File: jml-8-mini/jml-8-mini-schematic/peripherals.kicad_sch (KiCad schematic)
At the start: 8 parts, among them J2 SIO CHB, J3 UART, J4 CTC EXTRA LINES, U4 Z80 CTC, U5 Z80 SIO

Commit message: update info section of schematic
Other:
- company: https://github.com/jac-oblong/jml -> https://github.com/jac-oblong/JML
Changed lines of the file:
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@@
     (date "2023-10-02")
     (rev "A")
-    (company "https://github.com/jac-oblong/jml")
+    (company "https://github.com/jac-oblong/JML")
     (comment 1 "Design of Z80 based microcomputer")
     (comment 3 "Released under MIT License")

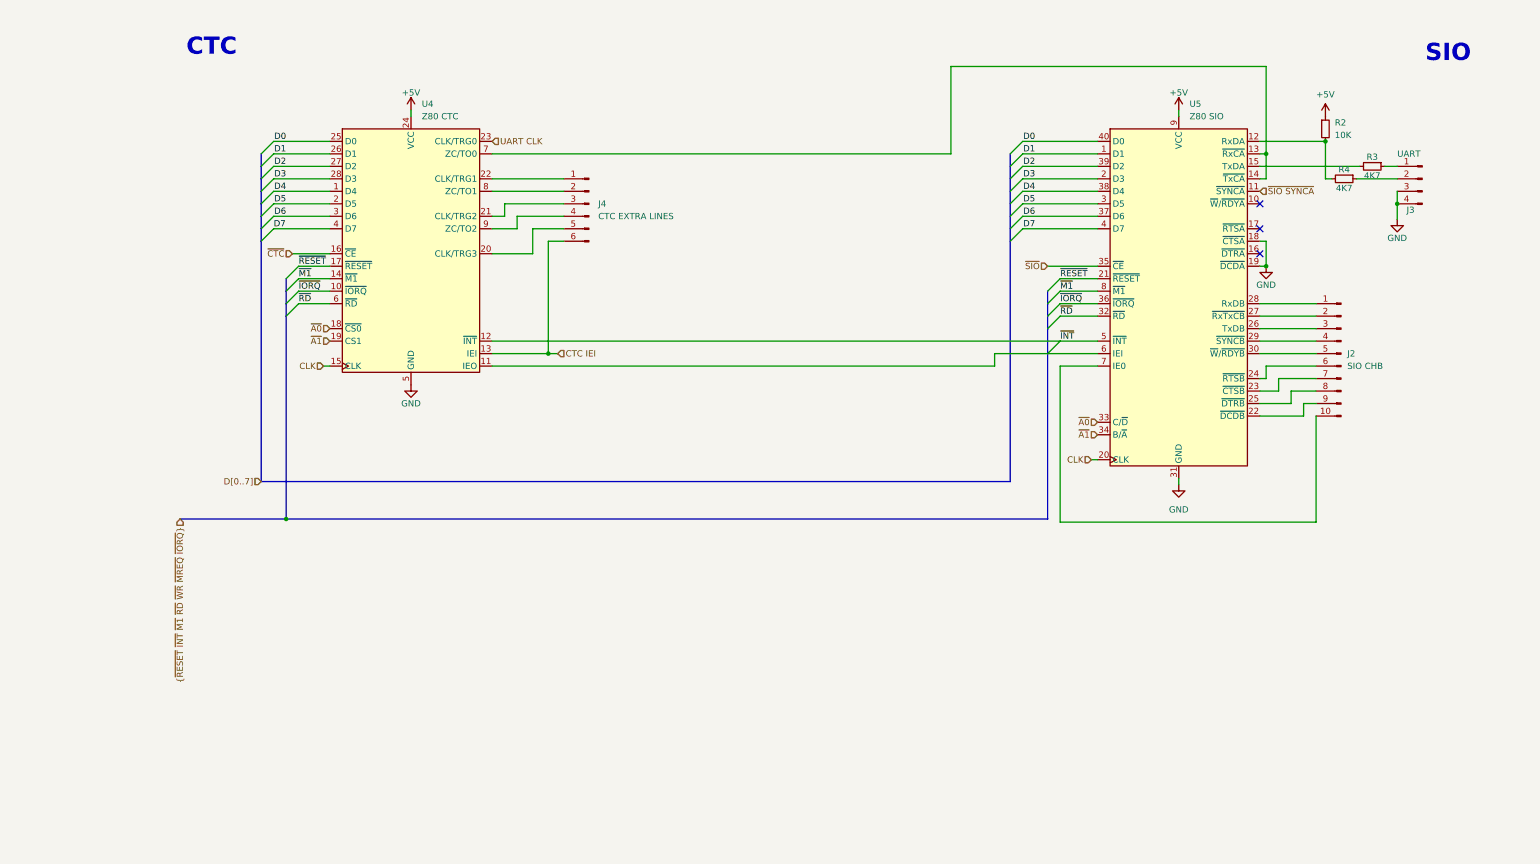
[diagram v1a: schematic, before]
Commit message: general "neatening" of schematics
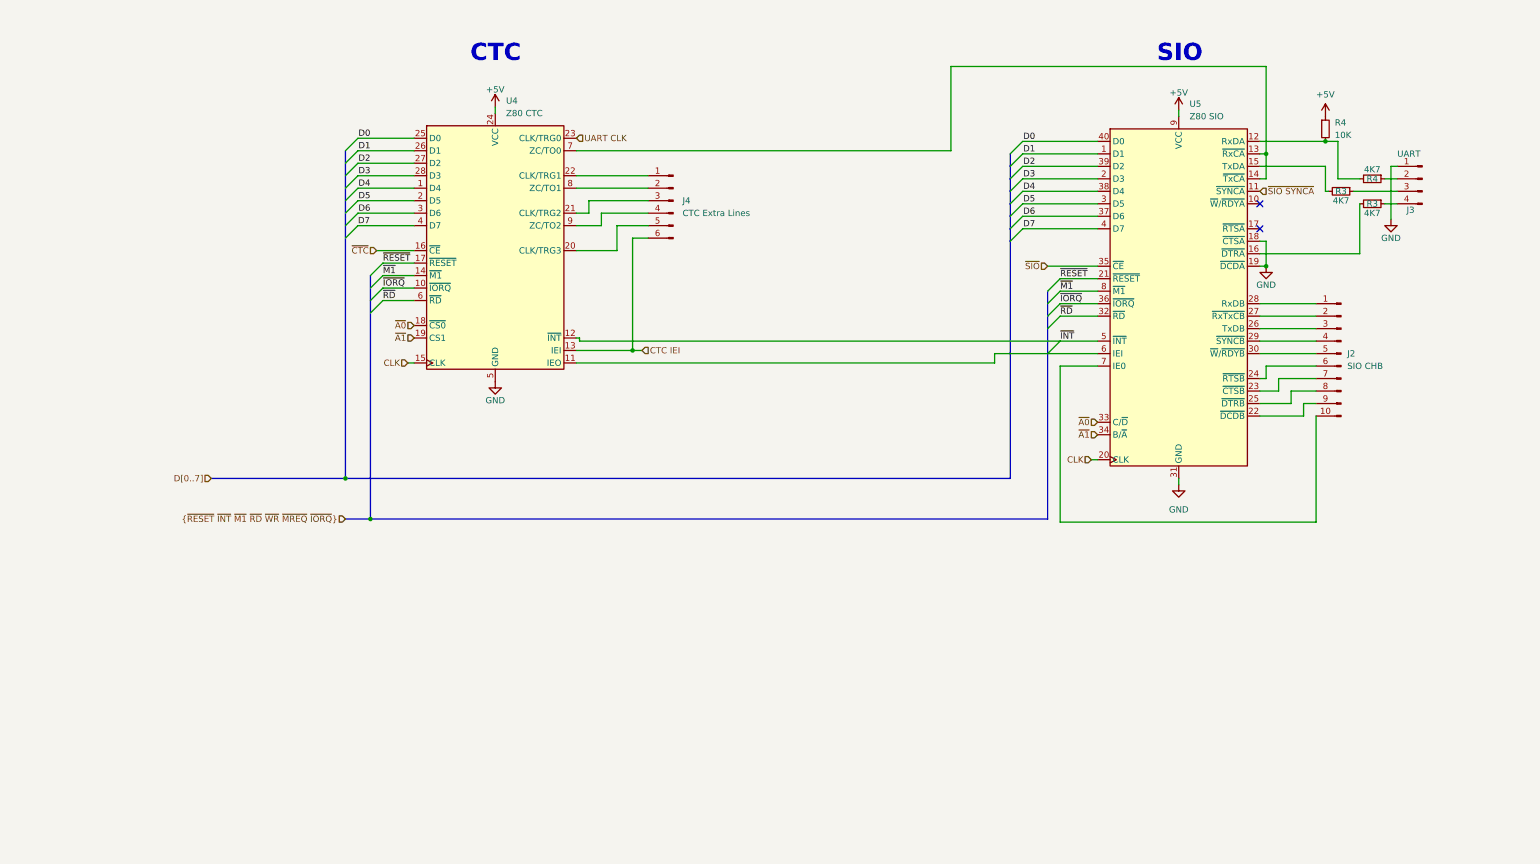
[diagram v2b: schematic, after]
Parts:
- added R3: 4K7, Resistor_THT:R_Axial_DIN0207_L6.3mm_D2.5mm_P10.16mm_Horizontal, symbol Device:R_Small
- J4: value CTC EXTRA LINES -> CTC Extra Lines
- renumbered R2 to R4
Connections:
- net GND: now also J3.1 (Pin_1); no longer J3.3 (Pin_3), J3.4 (Pin_4)
- net at R3.1: now also J3.3 (Pin_3); no longer J3.1 (Pin_1)
- net at U5.16 (~{DTRA}): now also R3.2
- new net: J3.4 (Pin_4), R3.1
- no-connect marks 3 -> 2
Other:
- moved on the sheet: J4, R3, R4, U4

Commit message: change some footprints
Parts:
- R3, R4: footprint Resistor_THT:R_Axial_DIN0207_L6.3mm_D2.5mm_P10.16mm_Horizontal -> Resistor_THT:R_Axial_DIN0207_L6.3mm_D2.5mm_P7.62mm_Horizontal
- U4: footprint Package_DIP:DIP-28_W15.24mm_LongPads -> Package_DIP:DIP-28_W15.24mm_Socket_LongPads
- U5: footprint Package_DIP:DIP-40_W15.24mm_LongPads -> Package_DIP:DIP-40_W15.24mm_Socket_LongPads
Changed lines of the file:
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@@
       (effects (font (size 1.27 1.27)))
     )
-    (property "Footprint" "Resistor_THT:R_Axial_DIN0207_L6.3mm_D2.5mm_P10.16mm_Horizontal" (at 257.81 51.435 0)
+    (property "Footprint" "Resistor_THT:R_Axial_DIN0207_L6.3mm_D2.5mm_P7.62mm_Horizontal" (at 257.81 51.435 0)
       (effects (font (size 1.27 1.27)) hide)
     )
@@
       (effects (font (size 1.27 1.27)))
     )
-    (property "Footprint" "Resistor_THT:R_Axial_DIN0207_L6.3mm_D2.5mm_P10.16mm_Horizontal" (at 257.81 46.355 0)
+    (property "Footprint" "Resistor_THT:R_Axial_DIN0207_L6.3mm_D2.5mm_P7.62mm_Horizontal" (at 257.81 46.355 0)
       (effects (font (size 1.27 1.27)) hide)
     )
@@
       (effects (font (size 1.27 1.27)) (justify left))
     )
-    (property "Footprint" "Resistor_THT:R_Axial_DIN0207_L6.3mm_D2.5mm_P10.16mm_Horizontal" (at 248.285 36.195 0)
+    (property "Footprint" "Resistor_THT:R_Axial_DIN0207_L6.3mm_D2.5mm_P7.62mm_Horizontal" (at 248.285 36.195 0)
       (effects (font (size 1.27 1.27)) hide)
     )
@@
       (effects (font (size 1.27 1.27)))
     )
-    (property "Footprint" "Resistor_THT:R_Axial_DIN0207_L6.3mm_D2.5mm_P10.16mm_Horizontal" (at 251.46 48.895 0)
+    (property "Footprint" "Resistor_THT:R_Axial_DIN0207_L6.3mm_D2.5mm_P7.62mm_Horizontal" (at 251.46 48.895 0)
       (effects (font (size 1.27 1.27)) hide)
     )
@@
       (effects (font (size 1.27 1.27)) (justify left))
     )
-    (property "Footprint" "Package_DIP:DIP-40_W15.24mm_LongPads" (at 224.79 81.915 0)
+    (property "Footprint" "Package_DIP:DIP-40_W15.24mm_Socket_LongPads" (at 224.79 81.915 0)
       (effects (font (size 1.27 1.27)) hide)
     )
@@
       (effects (font (size 1.27 1.27)) (justify left))
     )
-    (property "Footprint" "Package_DIP:DIP-28_W15.24mm_LongPads" (at 79.375 58.42 0)
-      (effects (font (size 1.27 1.27)) hide)
-    )
+    (property "Footprint" "Package_DIP:DIP-28_W15.24mm_Socket_LongPads" (at 79.375 58.42 0)
+      (effects (font (size 1.27 1.27)) hide)
+    )

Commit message: lots of updates to schematic to make pcb routing easier, start on pcb design
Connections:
- net UART_CTS: now reaches J3.4 (Pin_4), R3.1
- net ~{DTRA}: now reaches R3.2, U5.16 (~{DTRA})
- net UART_Tx: now reaches J3.2 (Pin_2), R4.1
- net RxDA: now reaches R4.2, R4.2, U5.12 (RxDA)
- net CLK/TRG1: now reaches J4.1 (Pin_1), U4.22 (CLK/TRG1)
- net ZC/TO1: now reaches J4.2 (Pin_2), U4.8 (ZC/TO1)
- net CLK/TRG2: now reaches J4.3 (Pin_3), U4.21 (CLK/TRG2)
- net CLK/TRG3: now reaches J4.4 (Pin_4)
- net CLK/TRG3: now also U4.20 (CLK/TRG3); no longer U4.9 (ZC/TO2)
- net ZC/TO2: now reaches J4.5 (Pin_5)
- net ZC/TO2: now also U4.9 (ZC/TO2); no longer U4.20 (CLK/TRG3)
- net UART_Rx: now reaches J3.3 (Pin_3), R3.1
- net TxDA: now reaches R3.2, U5.15 (TxDA)
- net CTC_IEO: now reaches J2.1 (Pin_1)
- net CTC_IEO: now also U5.7 (IE0); no longer U5.28 (RxDB)
- net ~{DCDB}: now reaches J2.10 (Pin_10)
- net ~{DCDB}: now also U5.22 (~{DCDB}); no longer U5.7 (IE0)
- net ~{RxTxCB}: now reaches U5.27 (~{RxTxCB})
- net ~{RxTxCB}: now also J2.5 (Pin_5); no longer J2.2 (Pin_2)
- net TxDB: now reaches U5.26 (TxDB)
- net TxDB: now also J2.6 (Pin_6); no longer J2.3 (Pin_3)
- net RxDB: now reaches J2.4 (Pin_4)
- net RxDB: now also U5.28 (RxDB); no longer U5.29 (~{SYNCB})
- net ~{W}/~{RDYB}: now reaches U5.30 (~{W}/~{RDYB})
- net ~{W}/~{RDYB}: now also J2.2 (Pin_2); no longer J2.5 (Pin_5)
- net ~{RTSB}: now reaches U5.24 (~{RTSB})
- net ~{RTSB}: now also J2.8 (Pin_8); no longer J2.6 (Pin_6)
- net ~{CTSB}: now reaches U5.23 (~{CTSB})
- net ~{CTSB}: now also J2.9 (Pin_9); no longer J2.7 (Pin_7)
- net ~{DTRB}: now reaches U5.25 (~{DTRB})
- net ~{DTRB}: now also J2.7 (Pin_7); no longer J2.8 (Pin_8)
- net SIO_UART_CLK: now reaches U4.7 (ZC/TO0), U5.13 (~{RxCA}), U5.14 (~{TxCA})
- net SIO_IEI: now reaches U4.11 (IEO), U5.6 (IEI)
- new net ~{SYNCB}: J2.3 (Pin_3), U5.29 (~{SYNCB})
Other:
- note added: "PERIPHERALS"
- note added: "Resistors limit current, and prevent one device from powering the other"
- moved on the sheet: J2, J3, J4, U4

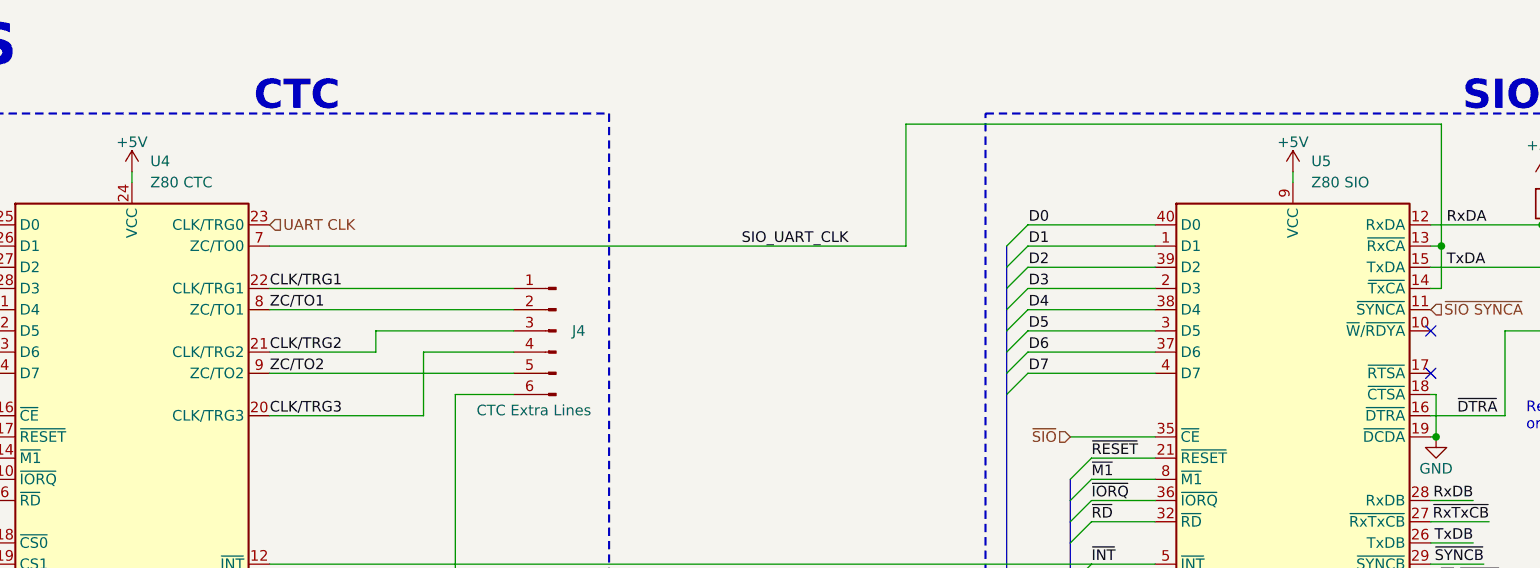
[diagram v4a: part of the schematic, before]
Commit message: complete PCB routing
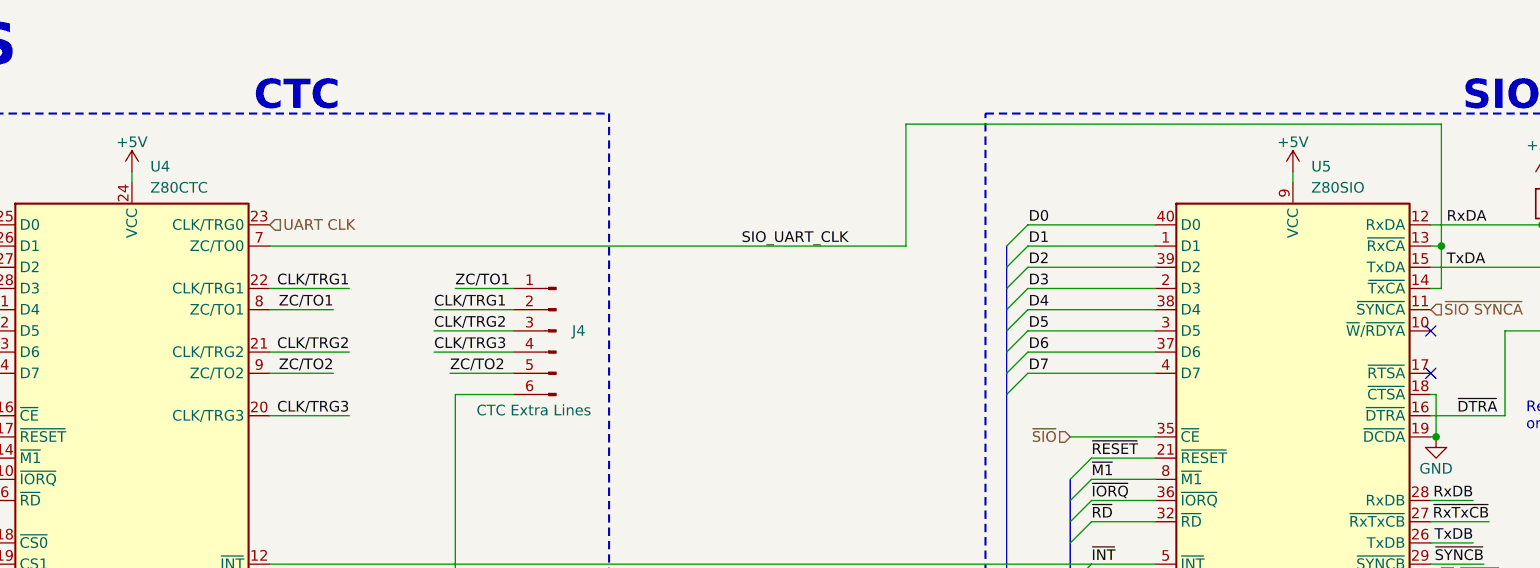
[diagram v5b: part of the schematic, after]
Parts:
- U4: value Z80 CTC -> Z80CTC
- U5: value Z80 SIO -> Z80SIO
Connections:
- net CLK/TRG1: now also J4.2 (Pin_2); no longer J4.1 (Pin_1)
- net ZC/TO1: now also J4.1 (Pin_1); no longer J4.2 (Pin_2)
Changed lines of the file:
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@@
-    (stroke (width 0) (type default))
-  )
-  (wire (pts (xy 114.3 61.595) (xy 95.885 61.595))
     (stroke (width 0) (type default))
   )
@@
     (stroke (width 0) (type default))
   )
-  (wire (pts (xy 95.885 46.355) (xy 125.095 46.355))
-    (stroke (width 0) (type default))
-  )
   (bus (pts (xy 48.895 107.315) (xy 48.895 59.055))
     (stroke (width 0) (type default))
@@
     (stroke (width 0) (type default))
   )
-  (wire (pts (xy 95.885 53.975) (xy 108.585 53.975))
-    (stroke (width 0) (type default))
-  )
   (bus (pts (xy 48.895 107.315) (xy 184.15 107.315))
     (stroke (width 0) (type default))
@@
     (stroke (width 0) (type default))
   )
-  (wire (pts (xy 95.885 48.895) (xy 125.095 48.895))
+  (wire (pts (xy 115.57 51.435) (xy 125.095 51.435))
     (stroke (width 0) (type default))
   )
@@
     (stroke (width 0) (type default))
   )
-  (wire (pts (xy 108.585 51.435) (xy 125.095 51.435))
-    (stroke (width 0) (type default))
-  )
   (wire (pts (xy 62.865 51.435) (xy 51.435 51.435))
     (stroke (width 0) (type default))
@@
     (stroke (width 0) (type default))
   )
+  (wire (pts (xy 115.57 48.895) (xy 125.095 48.895))
+    (stroke (width 0) (type default))
+  )
   (wire (pts (xy 56.515 64.135) (xy 62.865 64.135))
     (stroke (width 0) (type default))
@@
     (stroke (width 0) (type default))
   )
+  (wire (pts (xy 95.885 48.895) (xy 103.505 48.895))
+    (stroke (width 0) (type default))
+  )
   (wire (pts (xy 234.95 92.075) (xy 240.03 92.075))
     (stroke (width 0) (type default))
@@
     (stroke (width 0) (type default))
   )
+  (wire (pts (xy 117.475 56.515) (xy 125.095 56.515))
+    (stroke (width 0) (type default))
+  )
   (bus (pts (xy 48.895 46.355) (xy 48.895 48.895))
     (stroke (width 0) (type default))
@@
     (stroke (width 0) (type default))
   )
-  (wire (pts (xy 95.885 56.515) (xy 125.095 56.515))
+  (wire (pts (xy 95.885 53.975) (xy 105.41 53.975))
     (stroke (width 0) (type default))
   )
@@
     (stroke (width 0) (type default))
   )
+  (wire (pts (xy 115.57 53.975) (xy 125.095 53.975))
+    (stroke (width 0) (type default))
+  )
   (wire (pts (xy 248.285 43.815) (xy 234.95 43.815))
     (stroke (width 0) (type default))
@@
     (stroke (width 0) (type default))
   )
+  (wire (pts (xy 95.885 46.355) (xy 105.41 46.355))
+    (stroke (width 0) (type default))
+  )
   (wire (pts (xy 194.31 69.215) (xy 201.93 69.215))
     (stroke (width 0) (type default))
@@
     (stroke (width 0) (type default))
   )
-  (wire (pts (xy 108.585 53.975) (xy 108.585 51.435))
-    (stroke (width 0) (type default))
-  )
   (wire (pts (xy 260.985 92.075) (xy 255.27 92.075))
     (stroke (width 0) (type default))
   )
+  (wire (pts (xy 95.885 61.595) (xy 105.41 61.595))
+    (stroke (width 0) (type default))
+  )
   (wire (pts (xy 201.93 46.355) (xy 186.69 46.355))
     (stroke (width 0) (type default))
@@
     (stroke (width 0) (type default))
   )
+  (wire (pts (xy 118.11 46.355) (xy 125.095 46.355))
+    (stroke (width 0) (type default))
+  )
   (wire (pts (xy 254.635 76.835) (xy 260.985 76.835))
     (stroke (width 0) (type default))
   )
-  (wire (pts (xy 114.3 53.975) (xy 125.095 53.975))
-    (stroke (width 0) (type default))
-  )
-  (wire (pts (xy 114.3 53.975) (xy 114.3 61.595))
+  (wire (pts (xy 95.885 56.515) (xy 103.505 56.515))
     (stroke (width 0) (type default))
   )
@@
     (effects (font (size 1.27 1.27)) (justify left bottom))
   )
-  (label "CLK{slash}TRG3" (at 95.885 61.595 0) (fields_autoplaced)
-    (effects (font (size 1.27 1.27)) (justify left bottom))
+  (label "CLK{slash}TRG3" (at 105.41 61.595 180) (fields_autoplaced)
+    (effects (font (size 1.27 1.27)) (justify right bottom))
   )
   (label "D6" (at 189.23 53.975 180) (fields_autoplaced)
     (effects (font (size 1.27 1.27)) (justify right bottom))
   )
-  (label "CLK{slash}TRG2" (at 95.885 53.975 0) (fields_autoplaced)
-    (effects (font (size 1.27 1.27)) (justify left bottom))
+  (label "CLK{slash}TRG2" (at 105.41 53.975 180) (fields_autoplaced)
+    (effects (font (size 1.27 1.27)) (justify right bottom))
   )
   (label "TxDA" (at 236.855 43.815 0) (fields_autoplaced)
@@
     (effects (font (size 1.27 1.27)) (justify left bottom))
   )
+  (label "ZC{slash}TO1" (at 118.11 46.355 0) (fields_autoplaced)
+    (effects (font (size 1.27 1.27)) (justify left bottom))
+  )
   (label "D3" (at 189.23 46.355 180) (fields_autoplaced)
     (effects (font (size 1.27 1.27)) (justify right bottom))
@@
     (effects (font (size 1.27 1.27)) (justify right bottom))
   )
-  (label "ZC{slash}TO2" (at 95.885 56.515 0) (fields_autoplaced)
-    (effects (font (size 1.27 1.27)) (justify left bottom))
-  )
-  (label "CLK{slash}TRG1" (at 95.885 46.355 0) (fields_autoplaced)
-    (effects (font (size 1.27 1.27)) (justify left bottom))
+  (label "ZC{slash}TO2" (at 103.505 56.515 180) (fields_autoplaced)
+    (effects (font (size 1.27 1.27)) (justify right bottom))
+  )
+  (label "CLK{slash}TRG1" (at 105.41 46.355 180) (fields_autoplaced)
+    (effects (font (size 1.27 1.27)) (justify right bottom))
   )
   (label "~{IORQ}" (at 56.515 69.215 0) (fields_autoplaced)
@@
     (effects (font (size 1.27 1.27)) (justify left bottom))
   )
+  (label "CLK{slash}TRG3" (at 115.57 53.975 0) (fields_autoplaced)
+    (effects (font (size 1.27 1.27)) (justify left bottom))
+  )
   (label "D2" (at 189.23 43.815 180) (fields_autoplaced)
     (effects (font (size 1.27 1.27)) (justify right bottom))
@@
     (effects (font (size 1.27 1.27)) (justify right bottom))
   )
+  (label "ZC{slash}TO2" (at 117.475 56.515 0) (fields_autoplaced)
+    (effects (font (size 1.27 1.27)) (justify left bottom))
+  )
   (label "CTC_IEO" (at 194.31 84.455 0) (fields_autoplaced)
     (effects (font (size 1.27 1.27)) (justify left bottom))
@@
     (effects (font (size 1.27 1.27)) (justify right bottom))
   )
+  (label "CLK{slash}TRG1" (at 115.57 48.895 0) (fields_autoplaced)
+    (effects (font (size 1.27 1.27)) (justify left bottom))
+  )
   (label "SIO_UART_CLK" (at 152.4 41.275 0) (fields_autoplaced)
     (effects (font (size 1.27 1.27)) (justify left bottom))
@@
     (effects (font (size 1.27 1.27)) (justify left bottom))
   )
-  (label "ZC{slash}TO1" (at 95.885 48.895 0) (fields_autoplaced)
+  (label "ZC{slash}TO1" (at 103.505 48.895 180) (fields_autoplaced)
+    (effects (font (size 1.27 1.27)) (justify right bottom))
+  )
+  (label "CLK{slash}TRG2" (at 115.57 51.435 0) (fields_autoplaced)
     (effects (font (size 1.27 1.27)) (justify left bottom))
   )
@@
   (symbol (lib_id "jml-8-mini-library:Z80_SIO/0") (at 218.44 67.945 0) (unit 1)
     (in_bom yes) (on_board yes) (dnp no) (fields_autoplaced)
-    (property "Reference" "U5" (at 220.6341 31.115 0)
+    (property "Reference" "U5" (at 220.6341 31.75 0)
       (effects (font (size 1.27 1.27)) (justify left))
     )
-    (property "Value" "Z80 SIO" (at 220.6341 33.655 0)
+    (property "Value" "Z80SIO" (at 220.6341 34.29 0)
       (effects (font (size 1.27 1.27)) (justify left))
     )
@@
   (symbol (lib_id "jml-8-mini-library:Z80_CTC") (at 79.375 59.055 0) (unit 1)
     (in_bom yes) (on_board yes) (dnp no) (fields_autoplaced)
-    (property "Reference" "U4" (at 81.5691 31.115 0)
+    (property "Reference" "U4" (at 81.5691 31.75 0)
       (effects (font (size 1.27 1.27)) (justify left))
     )
-    (property "Value" "Z80 CTC" (at 81.5691 33.655 0)
+    (property "Value" "Z80CTC" (at 81.5691 34.29 0)
       (effects (font (size 1.27 1.27)) (justify left))
     )
